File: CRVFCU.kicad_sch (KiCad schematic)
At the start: 150 parts, among them J1 TagConnect_TC2030, J3 USB_C_Receptacle_USB2.0_16P, J4 Micro_SD_Card_Det2, Q3 DMG2301L, Q4 BC818, Q5 DMG2301L, Q6 DMG2301L, SW1 SW_Omron_B3FS, SW2 SW_Nidec_CAS-120A1, U1 MS5611-01BA, U10 W25Q128JVS, U11 CM1624, U13 USBLC6-2SC6, U14 USBLC6-2SC6, U15 MAX17049, U16 SI7232DN-T1, U17 SN74LV1T34DCK, U2 STM32H747IITx, U3 LIS2MDL, U4 ICM-45686, U5 FXMA108, U6 AP1117-50, U7 AP1117-33, U8 SI7232DN-T1, U9 USBLC6-4SC6, Y1 32.768khz, Y3 32.768khz, Y4 25MHZ

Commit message: completed 50x100 routing, attempting 40mm
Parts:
- added C40: 100nF, Capacitor_SMD:C_0402_1005Metric, symbol Device:C
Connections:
- net +8V4: now also C40.1
- net ALRT: now also U2.89 (PD8)
- net ARM: now also U2.110 (PG2); no longer U2.19 (PF1)
- net BUZZ: now also U2.148 (PD5); no longer U2.1 (PE2)
- net GND: now also C40.2
- net IMU_INT: now also U2.49 (PA4); no longer U2.46 (PA3)
- net PYC0: now also U2.149 (PD6); no longer U2.68 (PE8)
- net PYC1: now also U2.155 (PG11); no longer U2.72 (PE10)
- net PYC2: now also U2.156 (PG12); no longer U2.74 (PE12)
- net PYC3: now also U2.161 (PG15); no longer U2.76 (PE14)
- net PYO0: now also PYRO_TERM1.4 (Pin_4); no longer PYRO_TERM1.10 (Pin_10)
- net PYO1: now also PYRO_TERM1.5 (Pin_5); no longer PYRO_TERM1.4 (Pin_4)
- net PYO2: now also PYRO_TERM1.8 (Pin_8); no longer PYRO_TERM1.6 (Pin_6)
- net PYO3: now also PYRO_TERM1.9 (Pin_9); no longer PYRO_TERM1.8 (Pin_8)
- net PYR0: now also U2.150 (PD7); no longer U2.67 (PE7)
- net PYR1: now also U2.154 (PG10); no longer U2.69 (PE9)
- net PYR2: now also U2.157 (PG13); no longer U2.73 (PE11)
- net PYR3: now also U2.158 (PG14); no longer U2.75 (PE13)
- net RAD_CTS: now also U2.43 (PA2)
- net RAD_RTS: now also U2.46 (PA3)
- net RAD_RX: now also U2.42 (PA1); no longer U2.143 (PD0)
- net RAD_TX: now also U2.41 (PA0); no longer U2.144 (PD1)
- net SRVI_0: now also U2.128 (PA9); no longer U2.148 (PD5)
- net SRVI_1: now also U2.127 (PA8); no longer U2.149 (PD6)
- net SRVI_2: now also U2.123 (PC7); no longer U2.150 (PD7)
- net SRVI_3: now also U2.122 (PC6); no longer U2.153 (PG9)
- net SRVI_4: now also U2.118 (PG8); no longer U2.154 (PG10)
- net SRVI_5: now also U2.117 (PG7); no longer U2.155 (PG11)
- net SRVI_6: now also U2.115 (PG5); no longer U2.156 (PG12)
- net SRVI_7: now also U2.114 (PG4); no longer U2.157 (PG13)
- net SRV_OE: now also U2.129 (PA10); no longer U2.147 (PD4)
- net VIDEO: now also U2.111 (PG3); no longer U2.18 (PF0)
- net VPYRO: now also PYRO_TERM1.10 (Pin_10), PYRO_TERM1.6 (Pin_6); no longer PYRO_TERM1.5 (Pin_5), PYRO_TERM1.9 (Pin_9)
- new net: C13.1, U2.172 (VCAP)
- new net: C14.1, U2.133 (VCAP)
- now unconnected: U2.80 (VCAP)

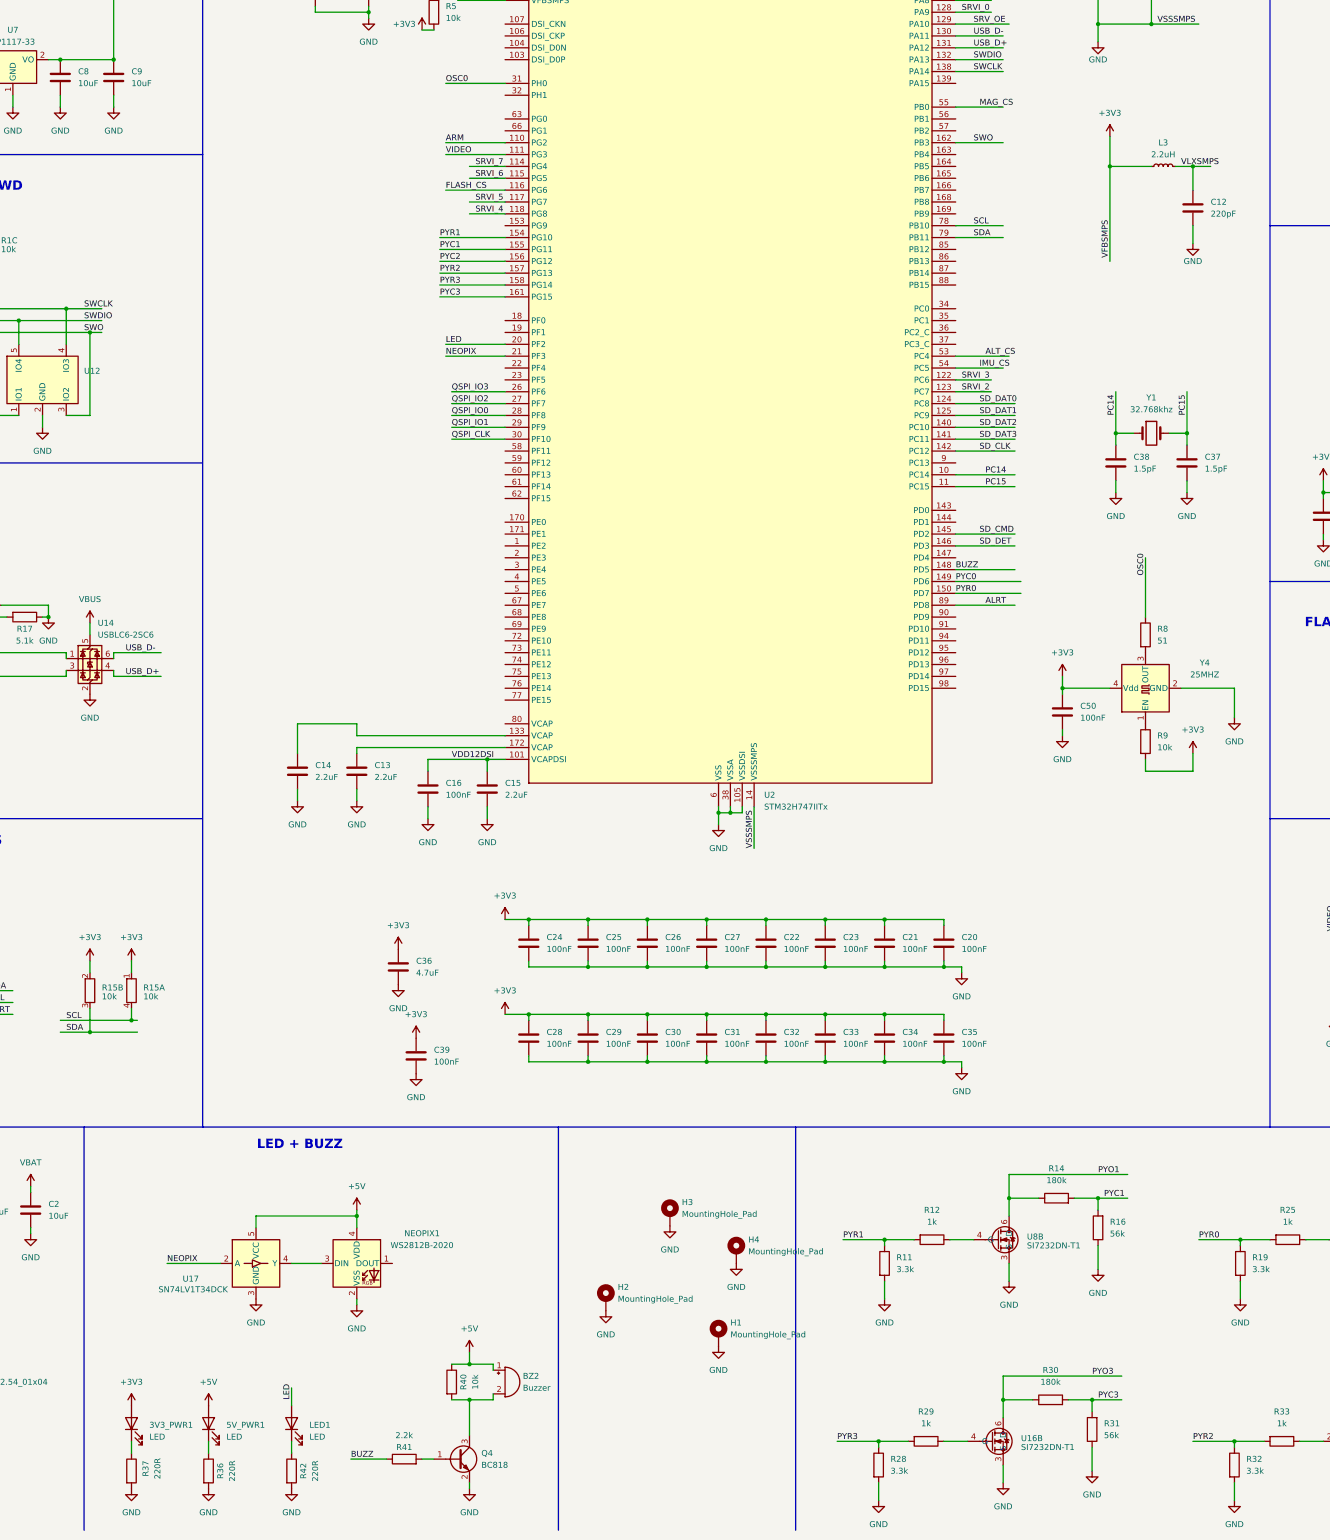
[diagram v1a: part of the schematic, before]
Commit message: added bom and changed 25mhz oscillator
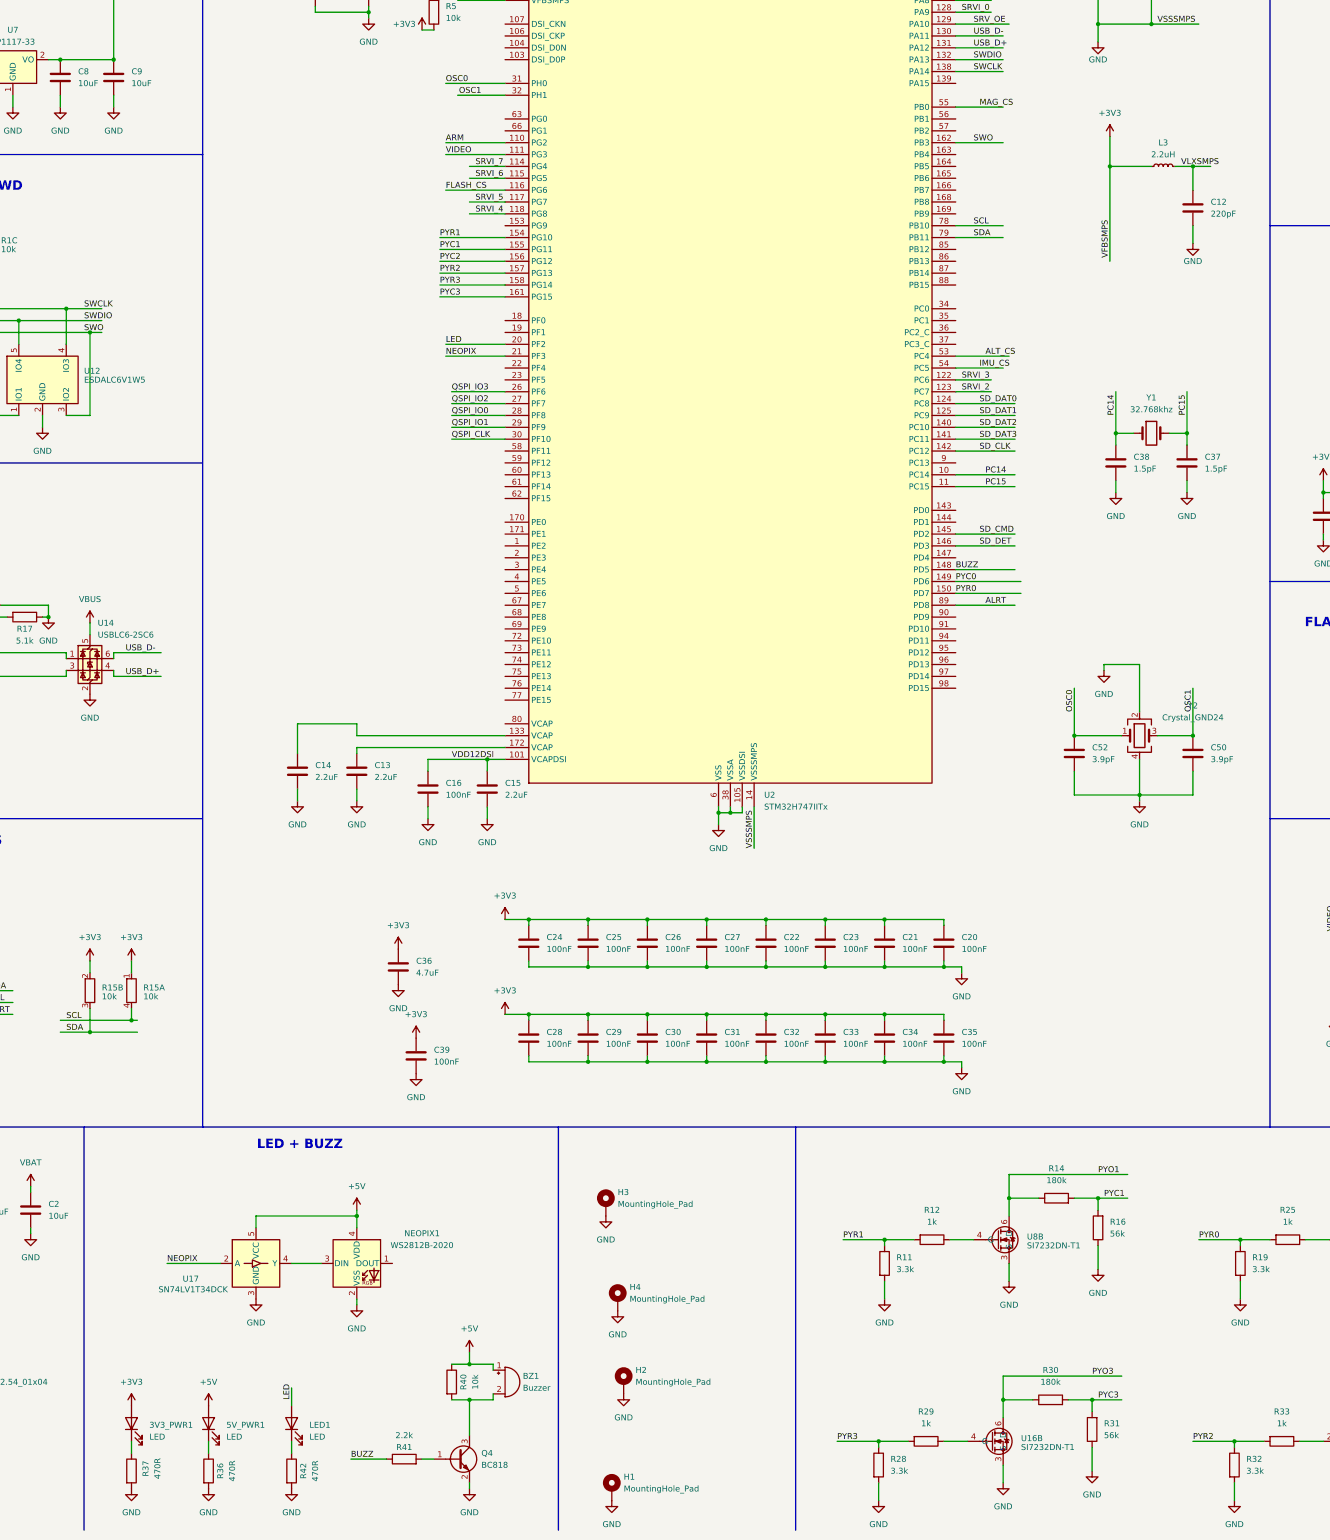
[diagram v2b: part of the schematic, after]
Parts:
- removed R8: 51, Resistor_SMD:R_0402_1005Metric, symbol Device:R
- removed R9: 10k, Resistor_SMD:R_0402_1005Metric, symbol Device:R
- removed Y4: 25MHZ, Oscillator:Oscillator_SMD_Abracon_ASE-4Pin_3.2x2.5mm, symbol Oscillator:ASE-xxxMHz
- added C52: 3.9pF, Capacitor_SMD:C_0402_1005Metric, symbol Device:C
- added Y2: Crystal_GND24, Crystal:Crystal_SMD_3225-4Pin_3.2x2.5mm, symbol Device:Crystal_GND24
- C50: value 100nF -> 3.9pF
- R36, R37, R42: value 220R -> 470R
- U12: value ~ -> ESDALC6V1W5
- U16, U8: footprint FCU2025Lib:SQJ500AEP-T1_GE3_VIS -> FCU2025Lib:PowerPak1212-8-Dual
- renumbered BZ2 to BZ1
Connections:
- net +3V3: no longer C50.1
- net GND: now also C52.2, Y2.2, Y2.4
- net OSC0: now also C52.1, Y2.1
- net OSC1: now reaches U2.32 (PH1)
- net OSC1: now also C50.1, Y2.3
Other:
- moved on the sheet: H1, H2, H3, H4
